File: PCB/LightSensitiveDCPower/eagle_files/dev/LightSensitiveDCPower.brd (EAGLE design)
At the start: 9 x 21 mm, 5 parts, among them SW1 PCM12SMTR

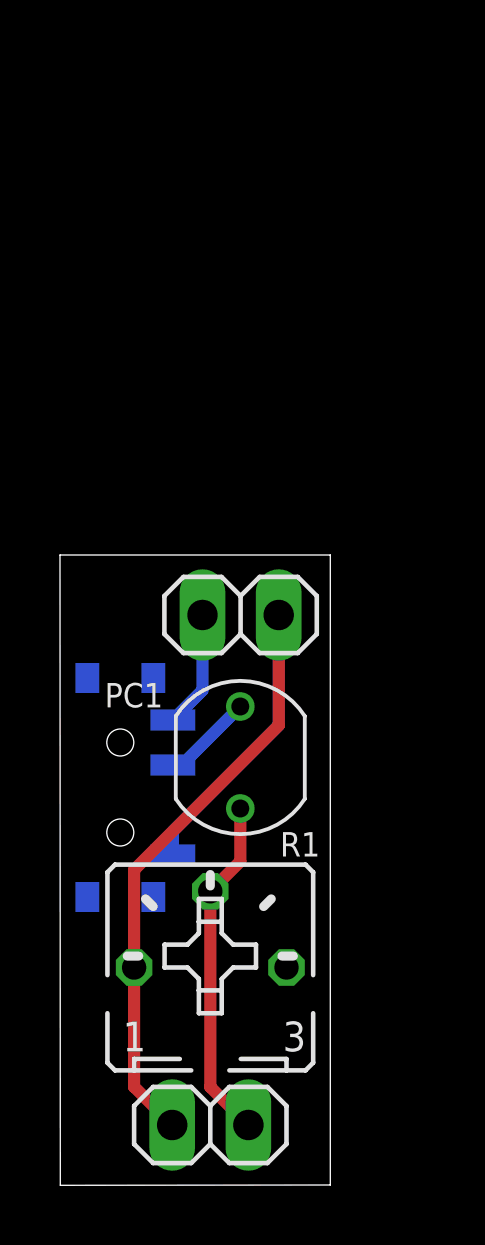
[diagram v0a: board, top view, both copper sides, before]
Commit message: New horizontal female header scheme for Light Sensitive DC power with dimensions adjusted accordingly.
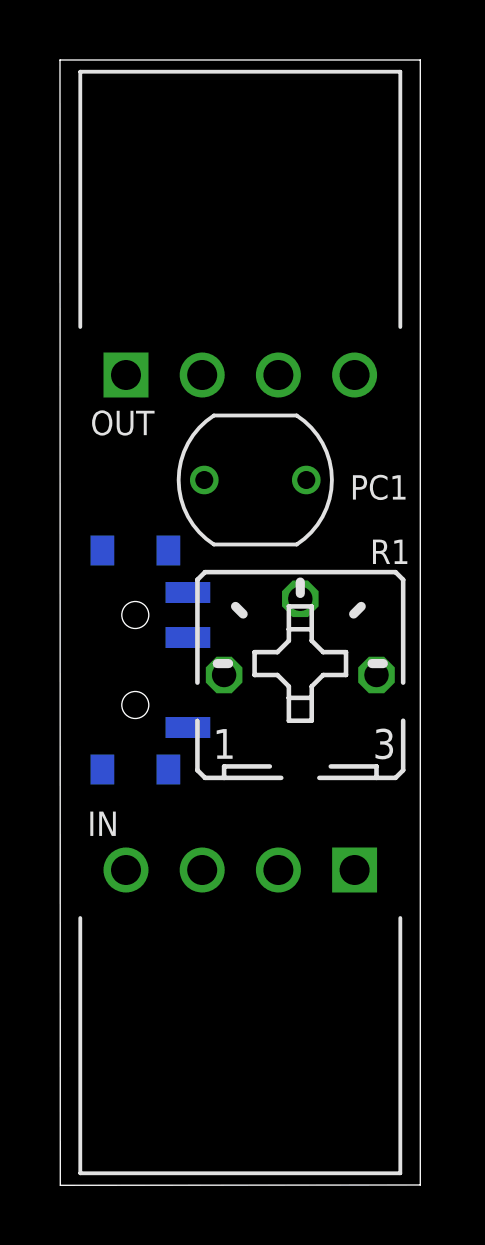
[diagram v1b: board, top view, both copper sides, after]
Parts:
- IN, OUT: device pinhead:1X02 -> SparkFun-Connectors:SULLIN-1X4_HORIZ
- moved OUT 25.0 mm to (6.00, 27.0)
- moved R1 10.2 mm to (8.00, 17.0)
- moved PC1 9.26 mm to (6.50, 23.5), turned to 90 degrees
- moved IN 8.50 mm to (6.00, 10.5)
- moved SW1 4.28 mm to (2.50, 17.5)
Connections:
- net N$1: now also IN.P$1, OUT.P$1; no longer IN.1, OUT.1
- net N$2: now also IN.P$4; no longer IN.2
- net N$4: now also OUT.P$4; no longer OUT.2
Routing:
- net N$1: track 29.0 -> 0.00 mm
- net N$4: track 11.5 -> 0.00 mm
- net N$2: track 3.91 -> 0.00 mm
- net N$3: track 3.06 -> 0.00 mm
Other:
- board size 9 x 21 mm -> 12 x 37.5 mm
- board text removed: "GND"
- board text removed: "VIN"
- board text removed: "VOUT"

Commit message: Rearranged components so that board is less long.
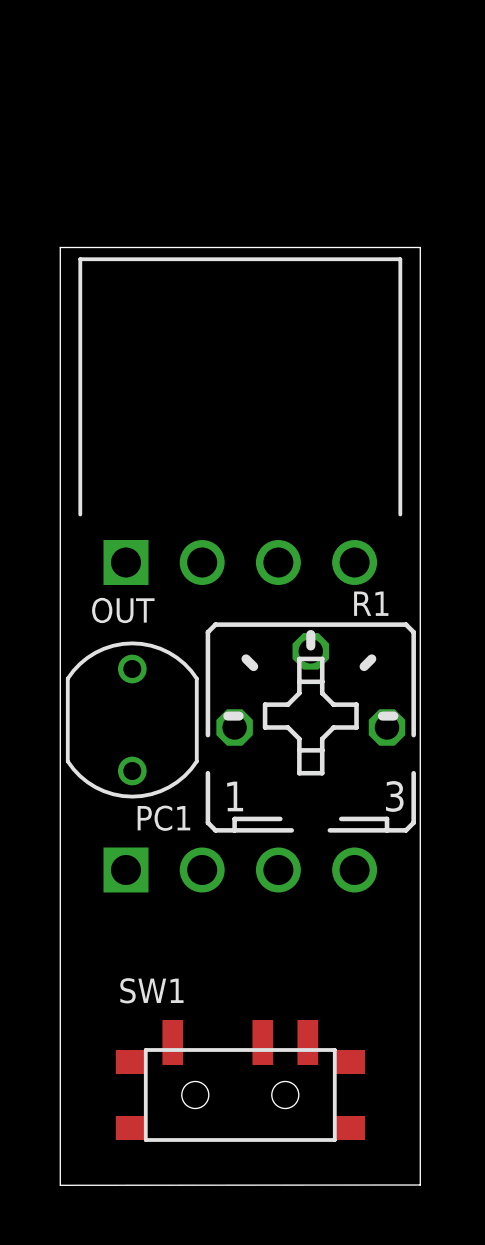
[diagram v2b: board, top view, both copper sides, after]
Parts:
- moved SW1 14.9 mm to (6.00, 3.00), flipped to the top, turned to 0 degrees
- moved PC1 8.99 mm to (2.40, 15.5), turned to 180 degrees
- moved OUT 6.25 mm to (6.00, 20.8)
- moved R1 1.78 mm to (8.35, 15.2)
- flipped IN to the bottom
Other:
- board size 12 x 37.5 mm -> 12 x 31.3 mm
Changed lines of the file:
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@@
 <plain>
 <wire x1="0" y1="-0.01" x2="12" y2="0" width="0" layer="20"/>
-<wire x1="12" y1="0" x2="12" y2="37.5" width="0" layer="20"/>
-<wire x1="12" y1="37.5" x2="-0.01" y2="37.5" width="0" layer="20"/>
-<wire x1="-0.01" y1="37.5" x2="0" y2="-0.01" width="0" layer="20"/>
-<text x="5.1" y="11.78" size="0.3048" layer="51">LiSePow
+<wire x1="12" y1="0" x2="12" y2="31.25" width="0" layer="20"/>
+<wire x1="12" y1="31.25" x2="0" y2="31.25" width="0" layer="20"/>
+<wire x1="0" y1="31.25" x2="0" y2="-0.01" width="0" layer="20"/>
+<text x="5.25" y="8" size="0.3048" layer="51">LiSePow
 Rev1
 09/27/14</text>
@@
 </autorouter>
 <elements>
-<element name="PC1" library="freddyLibr" package="PHOTOCELL_CERAMIC" value="" x="6.5" y="23.5" smashed="yes" rot="R90">
-<attribute name="NAME" x="11.6" y="23.66" size="0.8128" layer="25" rot="R180"/>
-</element>
-<element name="R1" library="pot" package="B25P" value="" x="8" y="17" smashed="yes">
-<attribute name="NAME" x="10.325" y="20.7" size="0.8128" layer="25" ratio="10"/>
-<attribute name="VALUE" x="4.8504" y="11.92" size="1.27" layer="27" ratio="10"/>
-</element>
-<element name="SW1" library="freddyLibr" package="PCM12SMTR" value="PCM12SMTR" x="2.5" y="17.5" smashed="yes" rot="MR90">
-<attribute name="NAME" x="3.13" y="22.13" size="0.8128" layer="26" rot="MR0"/>
-</element>
-<element name="IN" library="SparkFun-Connectors" package="SULLIN-1X4_HORIZ" value="" x="6" y="10.5" smashed="yes" rot="R180">
-<attribute name="NAME" x="0.9022" y="11.635" size="0.8128" layer="25"/>
-</element>
-<element name="OUT" library="SparkFun-Connectors" package="SULLIN-1X4_HORIZ" value="" x="6" y="27" smashed="yes">
-<attribute name="NAME" x="1.0022" y="24.995" size="0.8128" layer="25"/>
+<element name="PC1" library="freddyLibr" package="PHOTOCELL_CERAMIC" value="" x="2.4" y="15.5" smashed="yes" rot="R180">
+<attribute name="NAME" x="2.48" y="11.82" size="0.8128" layer="25"/>
+</element>
+<element name="R1" library="pot" package="B25P" value="" x="8.35" y="15.25" smashed="yes">
+<attribute name="NAME" x="9.695" y="18.97" size="0.8128" layer="25" ratio="10"/>
+<attribute name="VALUE" x="5.2004" y="10.17" size="1.27" layer="27" ratio="10"/>
+</element>
+<element name="SW1" library="freddyLibr" package="PCM12SMTR" value="PCM12SMTR" x="6" y="3" smashed="yes">
+<attribute name="NAME" x="4.2" y="6.88" size="0.8128" layer="25" rot="R180"/>
+</element>
+<element name="IN" library="SparkFun-Connectors" package="SULLIN-1X4_HORIZ" value="" x="6" y="10.5" smashed="yes" rot="MR180">
+<attribute name="NAME" x="11.0978" y="11.635" size="0.8128" layer="26" rot="MR0"/>
+</element>
+<element name="OUT" library="SparkFun-Connectors" package="SULLIN-1X4_HORIZ" value="" x="6" y="20.75" smashed="yes">
+<attribute name="NAME" x="1.0022" y="18.745" size="0.8128" layer="25"/>
 </element>
 </elements>
@@
 <contactref element="IN" pad="P$1"/>
 <contactref element="OUT" pad="P$1"/>
-<wire x1="9.81" y1="10.5" x2="2.19" y2="27" width="0" layer="19" extent="1-1"/>
-<wire x1="5.46" y1="17" x2="9.81" y2="10.5" width="0" layer="19" extent="1-1"/>
-<wire x1="4.25" y1="15.25" x2="5.46" y2="17" width="0" layer="19" extent="16-16"/>
+<wire x1="2.19" y1="10.5" x2="2.19" y2="20.75" width="0" layer="19" extent="1-1"/>
+<wire x1="5.81" y1="15.25" x2="2.19" y2="10.5" width="0" layer="19" extent="1-1"/>
+<wire x1="3.75" y1="4.75" x2="5.81" y2="15.25" width="0" layer="19" extent="16-16"/>
 </signal>
 <signal name="N$2">
 <contactref element="SW1" pad="3"/>
 <contactref element="IN" pad="P$4"/>
-<wire x1="2.19" y1="10.5" x2="4.25" y2="19.75" width="0" layer="19" extent="16-16"/>
+<wire x1="9.81" y1="10.5" x2="8.25" y2="4.75" width="0" layer="19" extent="16-16"/>
 </signal>
 <signal name="N$3">
 <contactref element="SW1" pad="2"/>
 <contactref element="PC1" pad="1"/>
-<wire x1="4.25" y1="18.25" x2="4.8" y2="23.5" width="0" layer="19" extent="16-16"/>
+<wire x1="6.75" y1="4.75" x2="2.4" y2="13.8" width="0" layer="19" extent="16-16"/>
 </signal>
 <signal name="N$4">
@@
 <contactref element="PC1" pad="2"/>
 <contactref element="OUT" pad="P$4"/>
-<wire x1="8" y1="19.54" x2="8.2" y2="23.5" width="0" layer="19" extent="1-1"/>
-<wire x1="9.81" y1="27" x2="8" y2="19.54" width="0" layer="19" extent="1-1"/>
+<wire x1="8.35" y1="17.79" x2="2.4" y2="17.2" width="0" layer="19" extent="1-1"/>
+<wire x1="9.81" y1="20.75" x2="8.35" y2="17.79" width="0" layer="19" extent="1-1"/>
 </signal>
 </signals>

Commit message: Routed and produced production files.
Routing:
- net N$1: track 0.00 -> 19.6 mm
- net N$3: track 0.00 -> 10.9 mm
- net N$4: track 0.00 -> 9.76 mm
- net N$2: track 0.00 -> 6.40 mm
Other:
- board text added: "LiSePow Rev2 12/2/14"
- board text removed: "LiSePow Rev1 09/27/14"
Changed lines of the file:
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@@
 <wire x1="12" y1="31.25" x2="0" y2="31.25" width="0" layer="20"/>
 <wire x1="0" y1="31.25" x2="0" y2="-0.01" width="0" layer="20"/>
-<text x="5.25" y="8" size="0.3048" layer="51">LiSePow
-Rev1
-09/27/14</text>
+<text x="6.12" y="7.92" size="0.3048" layer="51">LiSePow
+Rev2
+12/2/14</text>
 </plain>
 <attributes>
@@
 <elements>
 <element name="PC1" library="freddyLibr" package="PHOTOCELL_CERAMIC" value="" x="2.4" y="15.5" smashed="yes" rot="R180">
-<attribute name="NAME" x="2.48" y="11.82" size="0.8128" layer="25"/>
+<attribute name="NAME" x="0.68" y="11.9" size="0.8128" layer="25"/>
 </element>
 <element name="R1" library="pot" package="B25P" value="" x="8.35" y="15.25" smashed="yes">
@@
 </element>
 <element name="SW1" library="freddyLibr" package="PCM12SMTR" value="PCM12SMTR" x="6" y="3" smashed="yes">
-<attribute name="NAME" x="4.2" y="6.88" size="0.8128" layer="25" rot="R180"/>
+<attribute name="NAME" x="5.5" y="6.86" size="0.8128" layer="25" rot="R180"/>
 </element>
 <element name="IN" library="SparkFun-Connectors" package="SULLIN-1X4_HORIZ" value="" x="6" y="10.5" smashed="yes" rot="MR180">
-<attribute name="NAME" x="11.0978" y="11.635" size="0.8128" layer="26" rot="MR0"/>
+<attribute name="NAME" x="8.5278" y="12.035" size="0.8128" layer="26" rot="MR0"/>
 </element>
 <element name="OUT" library="SparkFun-Connectors" package="SULLIN-1X4_HORIZ" value="" x="6" y="20.75" smashed="yes">
@@
 <contactref element="IN" pad="P$1"/>
 <contactref element="OUT" pad="P$1"/>
-<wire x1="2.19" y1="10.5" x2="2.19" y2="20.75" width="0" layer="19" extent="1-1"/>
-<wire x1="5.81" y1="15.25" x2="2.19" y2="10.5" width="0" layer="19" extent="1-1"/>
-<wire x1="3.75" y1="4.75" x2="5.81" y2="15.25" width="0" layer="19" extent="16-16"/>
+<wire x1="2.19" y1="10.5" x2="5.81" y2="14.12" width="0.4064" layer="16"/>
+<wire x1="5.81" y1="14.12" x2="5.81" y2="15.25" width="0.4064" layer="16"/>
+<wire x1="3.75" y1="4.75" x2="2.19" y2="6.31" width="0.4064" layer="1"/>
+<wire x1="2.19" y1="6.31" x2="2.19" y2="10.5" width="0.4064" layer="1"/>
+<wire x1="5.81" y1="15.25" x2="5.81" y2="17.13" width="0.4064" layer="16"/>
+<wire x1="5.81" y1="17.13" x2="2.19" y2="20.75" width="0.4064" layer="16"/>
 </signal>
 <signal name="N$2">
 <contactref element="SW1" pad="3"/>
 <contactref element="IN" pad="P$4"/>
-<wire x1="9.81" y1="10.5" x2="8.25" y2="4.75" width="0" layer="19" extent="16-16"/>
+<wire x1="8.25" y1="4.75" x2="9.81" y2="6.31" width="0.4064" layer="1"/>
+<wire x1="9.81" y1="6.31" x2="9.81" y2="10.5" width="0.4064" layer="1"/>
 </signal>
 <signal name="N$3">
 <contactref element="SW1" pad="2"/>
 <contactref element="PC1" pad="1"/>
-<wire x1="6.75" y1="4.75" x2="2.4" y2="13.8" width="0" layer="19" extent="16-16"/>
+<wire x1="6.75" y1="4.75" x2="6.75" y2="5.95" width="0.4064" layer="1"/>
+<wire x1="6.75" y1="5.95" x2="3.48" y2="9.22" width="0.4064" layer="1"/>
+<wire x1="3.48" y1="9.22" x2="3.48" y2="12.72" width="0.4064" layer="1"/>
+<wire x1="3.48" y1="12.72" x2="2.4" y2="13.8" width="0.4064" layer="1"/>
 </signal>
 <signal name="N$4">
@@
 <contactref element="PC1" pad="2"/>
 <contactref element="OUT" pad="P$4"/>
-<wire x1="8.35" y1="17.79" x2="2.4" y2="17.2" width="0" layer="19" extent="1-1"/>
-<wire x1="9.81" y1="20.75" x2="8.35" y2="17.79" width="0" layer="19" extent="1-1"/>
+<wire x1="8.35" y1="17.79" x2="8.35" y2="19.29" width="0.4064" layer="1"/>
+<wire x1="8.35" y1="19.29" x2="9.81" y2="20.75" width="0.4064" layer="1"/>
+<wire x1="2.4" y1="17.2" x2="7.76" y2="17.2" width="0.4064" layer="1"/>
+<wire x1="7.76" y1="17.2" x2="8.35" y2="17.79" width="0.4064" layer="1"/>
 </signal>
 </signals>
